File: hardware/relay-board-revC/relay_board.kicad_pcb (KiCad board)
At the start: 4 copper layers, 174 x 110 mm, 157 parts, among them J1 USB_C_Receptacle_HRO_TYPE-C-3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, J10 Banana_Jack_1Pin, J11 Banana_Jack_1Pin, J12 Banana_Jack_1Pin, J13 Banana_Jack_1Pin, J14 Banana_Jack_1Pin, J15 Banana_Jack_1Pin, J16 Banana_Jack_1Pin, J17 Banana_Jack_1Pin, J6 BNC_Amphenol_B6252HB-NPP3G-50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, J7 BNC_Amphenol_B6252HB-NPP3G-50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, J8 PinHeader_2x05_P1.27mm_Vertic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, J9 BNC_Amphenol_B6252HB-NPP3G-50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, K1 G6K-2F-RF-S, K10 G6K-2F-RF-S, K11 G6K-2F-RF-S, K12 G6K-2F-RF-S, K13 G6K-2F-RF-S, K14 G6K-2F-RF-S, K15 G6K-2F-RF-S, K16 G6K-2F-RF-S, K17 G6K-2F-RF-S, K18 G6K-2F-RF-S, K19 G6K-2F-RF-S, K2 G6K-2F-RF-S, K20 G6K-2F-RF-S, K21 G6K-2F-RF-S, K22 G6K-2F-RF-S, K23 G6K-2F-RF-S, K3 G6K-2F-RF-S, K4 G6K-2F-RF-S, K5 G6K-2F-RF-S, K6 G6K-2F-RF-S, K7 G6K-2F-RF-S, K8 G6K-2F-RF-S, K9 G6K-2F-RF-S, SW1 SW_SPST_TL3342, SW2 SW_SPST_TL3342, U1 LQFP-48_7x7mm_P0.5mm, U10 SOT-23-5, U11 SOT-23-5, U12 WSON-6-1EP_2x2mm_P0.65mm_EP1x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, U2 SOIC-16_3.9x9.9mm_P1.27mm, U3 SOIC-16_3.9x9.9mm_P1.27mm, U4 SOIC-16_3.9x9.9mm_P1.27mm, U5 SOT-23-5, U6 SOIC-16_3.9x9.9mm_P1.27mm, U7 SOT-23-5, U8 SOT-23-5, U9 SOT-23-5

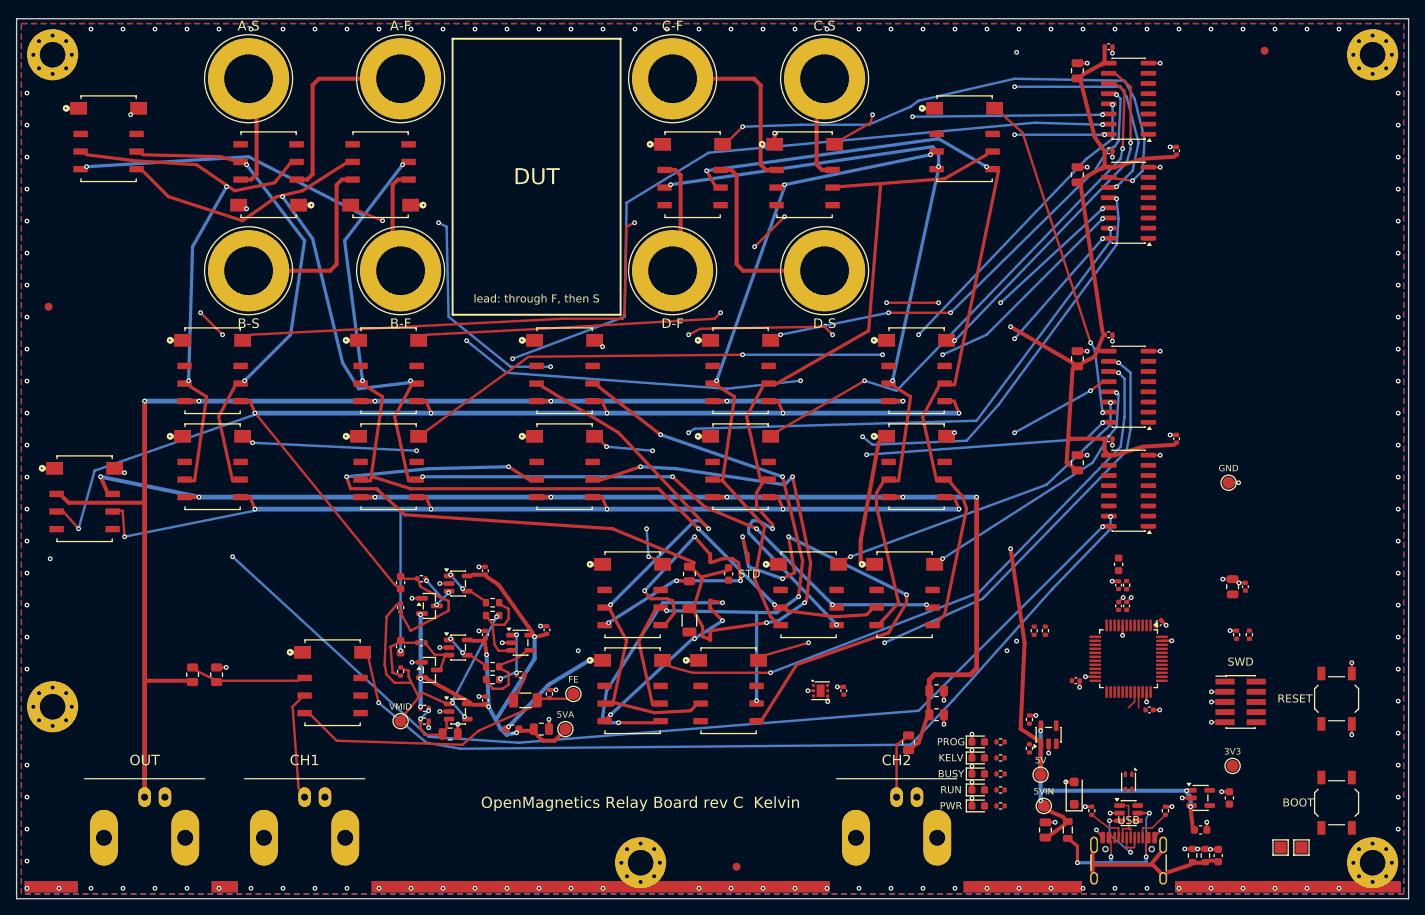
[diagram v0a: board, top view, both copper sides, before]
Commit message: Rev C as built: design, fab and JLC files of the manufactured boards
Schematic, routed PCB, netlist, generator/router scripts and docs as sent
to JLCPCB (fab outputs of 2026-10-13), Grayhill 02-21 clip footprint, the
via-out-of-pad fixes, the driven-guard study, BOM, JLC BOM/CPL, the fab
bundle and the review zip for N. Rosano. relay_map_revc.h is the map
generated from this schematic, checked against the netlist and flashed on
both built boards (firmware 2.0.0).

Co-Authored-By: Claude Opus 5.5 <noreply@anthropic.com>
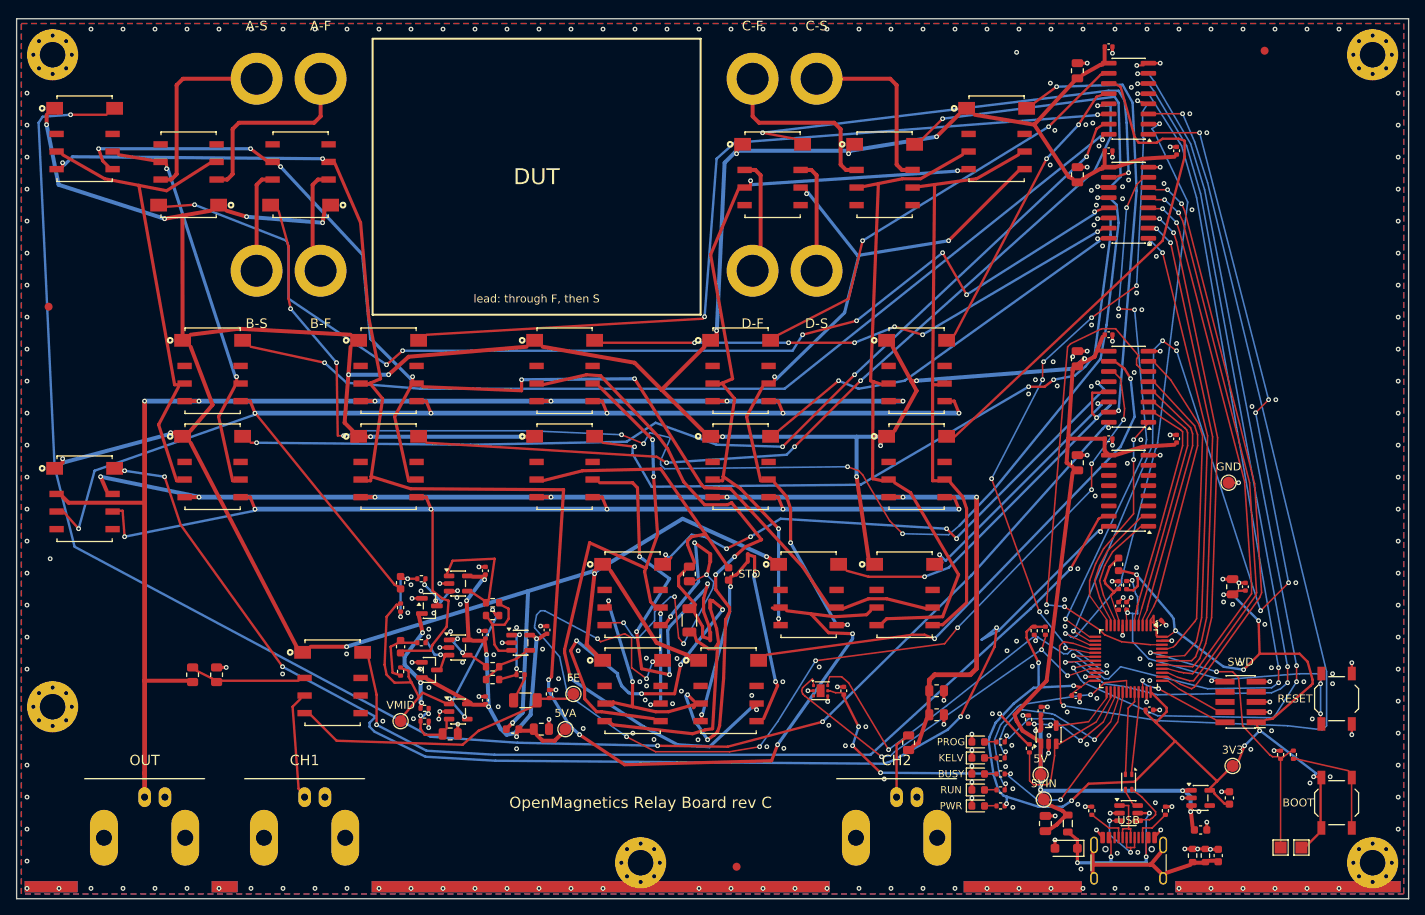
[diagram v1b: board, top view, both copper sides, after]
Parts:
- added C37: C_0402_1005Metric, C_0402_1005Metric, F.Cu at (168.1, 126.5)
- J10, J11, J12, J13, J14, J15, J16, J17: value Banana_Jack_1Pin -> Grayhill 02-21; footprint Banana_Jack_1Pin -> Grayhill_02-21_BananaPlug_4mm
- moved K5 22.0 mm to (152.5, 84.0)
- moved K6 22.0 mm to (152.5, 96.0)
- moved K7 22.0 mm to (130.5, 84.0)
- moved K8 22.0 mm to (130.5, 96.0)
- moved R17 16.0 mm to (199.6, 132.0)
- moved R4 16.0 mm to (198.0, 132.0)
- moved K17 12.0 mm to (151.0, 112.0)
- moved K18 12.0 mm to (139.0, 112.0)
- moved J10 10.0 mm to (78.0, 47.5)
- moved J12 10.0 mm to (78.0, 71.5)
- moved J14 10.0 mm to (132.0, 47.5)
- moved J16 10.0 mm to (132.0, 71.5)
- moved K11 10.0 mm to (61.5, 59.5)
- moved K12 10.0 mm to (75.5, 59.5)
- moved K13 10.0 mm to (148.5, 59.5)
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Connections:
- U1 pad 10: /GPIO15 -> /GPIO22
- U1 pad 12: /GPIO22 -> /GPIO15
- U1 pad 2: unconnected-(U1-PC13-Pad2) -> /GPIO19
- U1 pad 3: /GPIO19 -> /GPIO18
- U1 pad 4: /GPIO18 -> /GPIO17
- U1 pad 5: /GPIO17 -> /GPIO16
- U1 pad 6: /GPIO16 -> unconnected-(U1-PF1-Pad6)
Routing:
- net /+3V3: track 0.00 -> 201.4 mm, vias 0 -> 16
- net /GPIO1: track 0.00 -> 146.8 mm, vias 0 -> 8
- net /GPIO3: track 0.00 -> 127.9 mm, vias 0 -> 2
- net /GPIO7: track 0.00 -> 116.3 mm, vias 0 -> 4
- net /GPIO6: track 0.00 -> 112.9 mm, vias 0 -> 4
- net /GPIO5: track 0.00 -> 109.0 mm, vias 0 -> 4
- net /+5V: track 670.5 -> 563.8 mm, vias 26 -> 23
- net /GPIO4: track 0.00 -> 82.7 mm, vias 0 -> 8
- net /GPIO2: track 0.00 -> 75.3 mm, vias 0 -> 2
- net /GPIO13: track 0.00 -> 72.8 mm, vias 0 -> 2
- net /GPIO12: track 0.00 -> 69.9 mm, vias 0 -> 2
- net /K15_COIL: track 146.5 -> 214.5 mm, vias 5 -> 4
- net /GPIO11: track 0.00 -> 67.2 mm, vias 0 -> 2
- net /GPIO14: track 0.00 -> 63.9 mm, vias 0 -> 4
- net /GPIO10: track 0.00 -> 62.2 mm, vias 0 -> 2
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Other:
- board text added: "OpenMagnetics Relay Board rev C"
- board text removed: "OpenMagnetics Relay Board rev C Kelvin"
